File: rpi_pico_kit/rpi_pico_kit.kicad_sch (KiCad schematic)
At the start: 29 parts, among them J1 Barrel_Jack_Switch, J2 Conn_01x03_Male, Q1 BC807, Q2 BC807, SW1 SW_Push, U1 RPi Pico

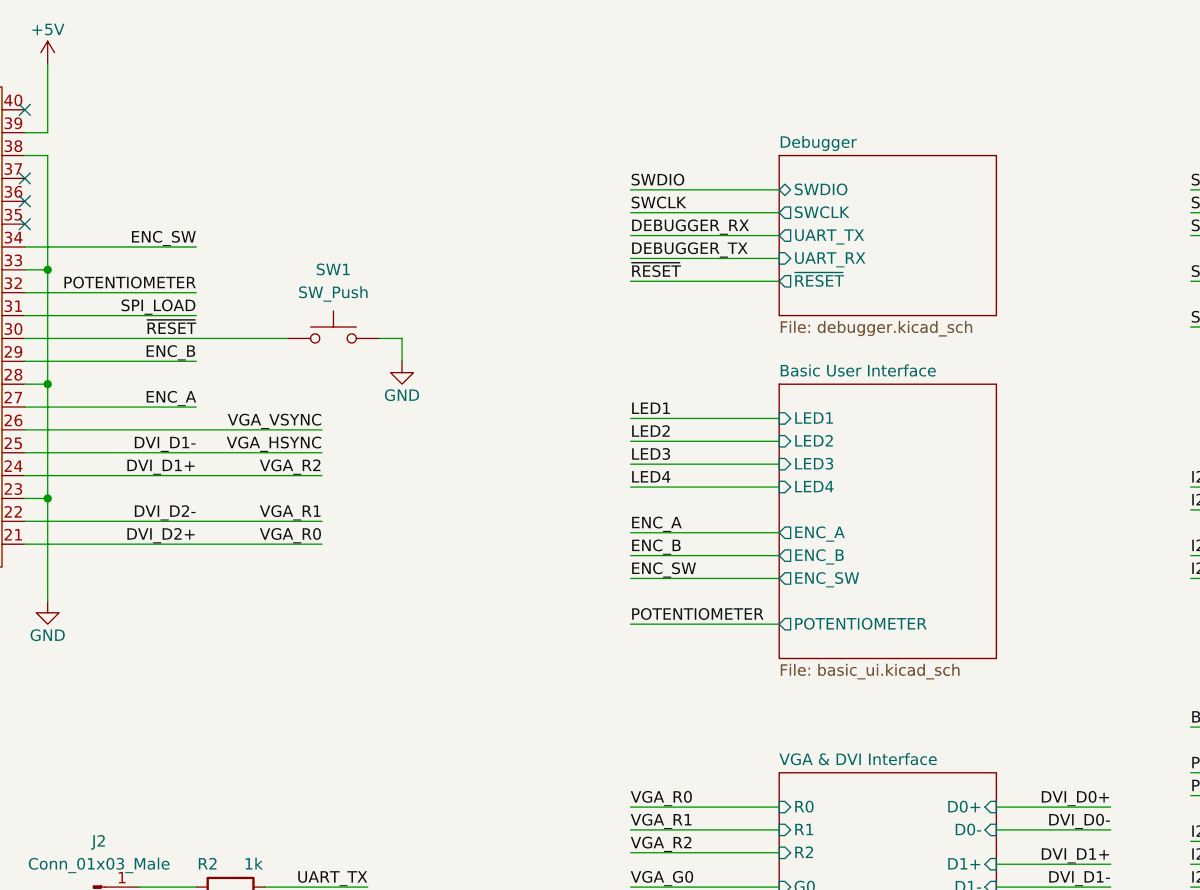
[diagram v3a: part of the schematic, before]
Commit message: added dac buttons
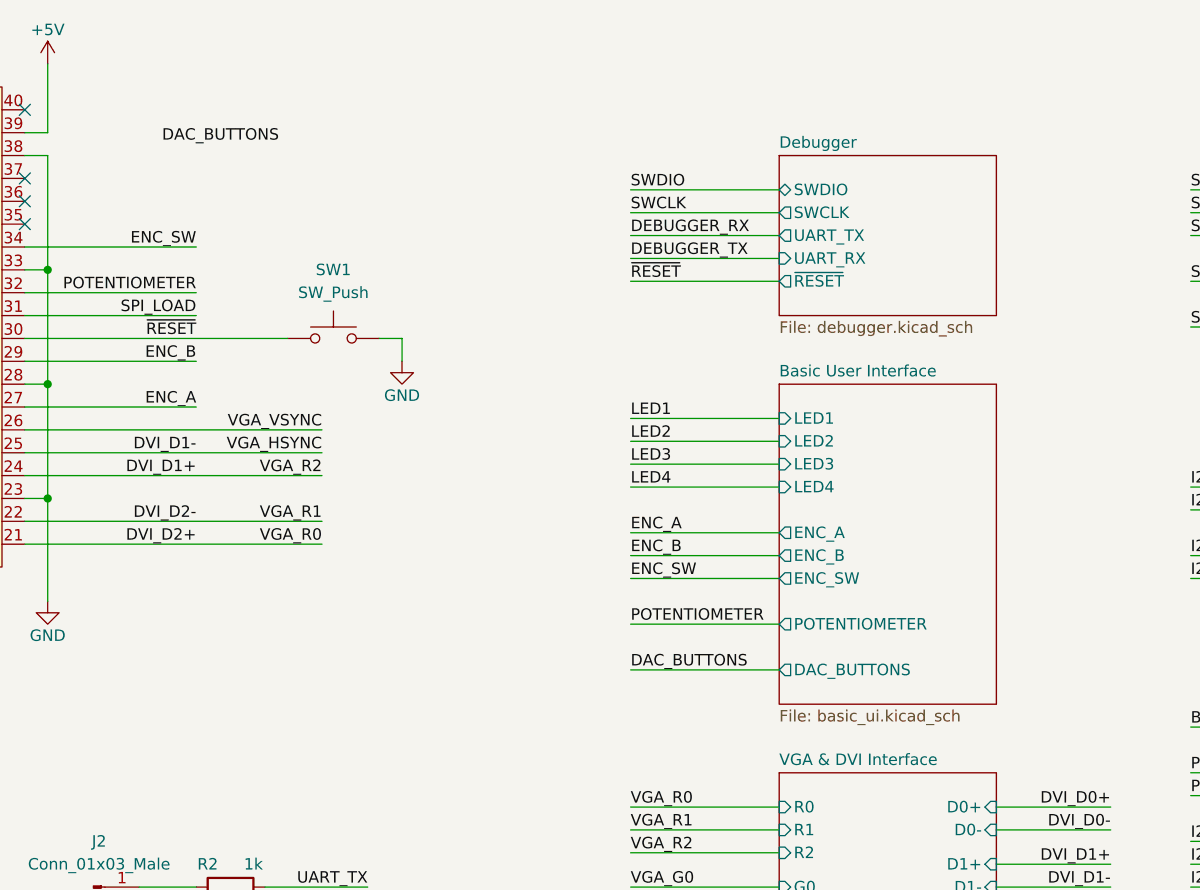
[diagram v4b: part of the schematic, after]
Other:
- sheet Basic User Interface ports: added DAC_BUTTONS; removed none
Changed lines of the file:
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@@
+    (stroke (width 0) (type default))
+  )
+  (wire (pts (xy 171.45 91.44) (xy 187.96 91.44))
     (stroke (width 0) (type default))
   )
@@
     (effects (font (size 1.27 1.27)) (justify left bottom))
   )
+  (label "DAC_BUTTONS" (at 171.45 91.44 0) (fields_autoplaced)
+    (effects (font (size 1.27 1.27)) (justify left bottom))
+  )
   (label "I2S_DIN" (at 53.34 62.23 0) (fields_autoplaced)
     (effects (font (size 1.27 1.27)) (justify left bottom))
   )
   (label "LED3" (at 27.94 54.61 0) (fields_autoplaced)
+    (effects (font (size 1.27 1.27)) (justify left bottom))
+  )
+  (label "DAC_BUTTONS" (at 119.38 33.02 0) (fields_autoplaced)
     (effects (font (size 1.27 1.27)) (justify left bottom))
   )
@@
     )
   )
-  (sheet (at 187.96 59.69) (size 24.13 30.48) (fields_autoplaced)
+  (sheet (at 187.96 59.69) (size 24.13 35.56) (fields_autoplaced)
     (stroke (width 0.1524) (type solid))
     (fill (color 0 0 0 0.0000))
@@
       (effects (font (size 1.27 1.27)) (justify left bottom))
     )
-    (property "Sheetfile" "basic_ui.kicad_sch" (id 1) (at 187.96 90.7546 0)
+    (property "Sheetfile" "basic_ui.kicad_sch" (id 1) (at 187.96 95.8346 0)
       (effects (font (size 1.27 1.27)) (justify left top))
     )
@@
     )
     (pin "LED4" input (at 187.96 71.12 180)
+      (effects (font (size 1.27 1.27)) (justify left))
+    )
+    (pin "DAC_BUTTONS" output (at 187.96 91.44 180)
       (effects (font (size 1.27 1.27)) (justify left))
     )
@@
       (reference "#PWR0147") (unit 1) (value "+5V") (footprint "")
     )
+    (path "/81612aa8-1e7d-439d-a45b-52594d29b291/1f6ded43-9f8d-4c63-8d4b-0b4527732d33"
+      (reference "#PWR?") (unit 1) (value "GND") (footprint "")
+    )
+    (path "/81612aa8-1e7d-439d-a45b-52594d29b291/4a31351e-1acf-47a2-a2c6-af92ae80f078"
+      (reference "#PWR?") (unit 1) (value "+3.3V") (footprint "")
+    )
+    (path "/81612aa8-1e7d-439d-a45b-52594d29b291/6f3c9916-5dd9-4b05-a345-f5527efc569b"
+      (reference "#PWR?") (unit 1) (value "+3.3V") (footprint "")
+    )
+    (path "/81612aa8-1e7d-439d-a45b-52594d29b291/89d0b3a4-37ce-4d00-9351-a681f8038582"
+      (reference "#PWR?") (unit 1) (value "GND") (footprint "")
+    )
+    (path "/81612aa8-1e7d-439d-a45b-52594d29b291/91069285-3fa6-4ca9-adec-5c5881e6c697"
+      (reference "#PWR?") (unit 1) (value "+3.3V") (footprint "")
+    )
+    (path "/81612aa8-1e7d-439d-a45b-52594d29b291/93d31bcb-10f6-4d54-bcae-9ef54872bd7b"
+      (reference "#PWR?") (unit 1) (value "+3.3V") (footprint "")
+    )
+    (path "/81612aa8-1e7d-439d-a45b-52594d29b291/ccea0e9a-8628-441a-ad2f-eb21f69a892a"
+      (reference "#PWR?") (unit 1) (value "+3.3V") (footprint "")
+    )
+    (path "/81612aa8-1e7d-439d-a45b-52594d29b291/f1a935b6-4bab-4abf-939e-7e028c183d62"
+      (reference "#PWR?") (unit 1) (value "GND") (footprint "")
+    )
     (path "/2bd19bd1-2975-4b91-a884-8b1113539e97/a927f1f4-98ba-40b8-bb8d-0eaab95070e5"
       (reference "BZ1") (unit 1) (value "Buzzer") (footprint "")
@@
       (reference "R89") (unit 1) (value "10k") (footprint "Resistor_SMD:R_0805_2012Metric_Pad1.20x1.40mm_HandSolder")
     )
+    (path "/81612aa8-1e7d-439d-a45b-52594d29b291/1ccb7d27-d1f4-4fcf-8a7f-33401111202f"
+      (reference "R?") (unit 1) (value "2k") (footprint "Resistor_SMD:R_0805_2012Metric_Pad1.20x1.40mm_HandSolder")
+    )
+    (path "/81612aa8-1e7d-439d-a45b-52594d29b291/39d89e3b-dd07-4df3-a868-bac27e6d5d7e"
+      (reference "R?") (unit 1) (value "1k") (footprint "Resistor_SMD:R_0805_2012Metric_Pad1.20x1.40mm_HandSolder")
+    )
+    (path "/81612aa8-1e7d-439d-a45b-52594d29b291/3c63107b-5d02-4b12-beac-ffe711ccd42d"
+      (reference "R?") (unit 1) (value "2k") (footprint "Resistor_SMD:R_0805_2012Metric_Pad1.20x1.40mm_HandSolder")
+    )
+    (path "/81612aa8-1e7d-439d-a45b-52594d29b291/42e543ad-9542-439b-9ff0-36e26f10ac03"
+      (reference "R?") (unit 1) (value "1k") (footprint "Resistor_SMD:R_0805_2012Metric_Pad1.20x1.40mm_HandSolder")
+    )
+    (path "/81612aa8-1e7d-439d-a45b-52594d29b291/4f8cb727-e4f9-46df-b234-ffef72cf20e7"
+      (reference "R?") (unit 1) (value "1k") (footprint "Resistor_SMD:R_0805_2012Metric_Pad1.20x1.40mm_HandSolder")
+    )
+    (path "/81612aa8-1e7d-439d-a45b-52594d29b291/5afb1b53-edfe-444c-9875-f83bd7c4a79d"
+      (reference "R?") (unit 1) (value "1k") (footprint "Resistor_SMD:R_0805_2012Metric_Pad1.20x1.40mm_HandSolder")
+    )
+    (path "/81612aa8-1e7d-439d-a45b-52594d29b291/6c7cd42a-7061-4c4b-9b98-0416e8fc4942"
+      (reference "R?") (unit 1) (value "2k") (footprint "Resistor_SMD:R_0805_2012Metric_Pad1.20x1.40mm_HandSolder")
+    )
+    (path "/81612aa8-1e7d-439d-a45b-52594d29b291/930f9912-8993-4e09-a189-56f2af054baf"
+      (reference "R?") (unit 1) (value "2k") (footprint "Resistor_SMD:R_0805_2012Metric_Pad1.20x1.40mm_HandSolder")
+    )
+    (path "/81612aa8-1e7d-439d-a45b-52594d29b291/c31321a7-a23c-41d8-914c-d144675613f4"
+      (reference "R?") (unit 1) (value "1k") (footprint "Resistor_SMD:R_0805_2012Metric_Pad1.20x1.40mm_HandSolder")
+    )
+    (path "/81612aa8-1e7d-439d-a45b-52594d29b291/cef2fd18-09ac-4f1b-8146-114e1991c8c7"
+      (reference "R?") (unit 1) (value "1k") (footprint "Resistor_SMD:R_0805_2012Metric_Pad1.20x1.40mm_HandSolder")
+    )
+    (path "/81612aa8-1e7d-439d-a45b-52594d29b291/e207b25f-a59c-43cc-b016-0dae5a5059ef"
+      (reference "R?") (unit 1) (value "2k") (footprint "Resistor_SMD:R_0805_2012Metric_Pad1.20x1.40mm_HandSolder")
+    )
+    (path "/81612aa8-1e7d-439d-a45b-52594d29b291/ef3534a4-6f90-4e7a-8bb9-e00ba3d1809e"
+      (reference "R?") (unit 1) (value "1k") (footprint "Resistor_SMD:R_0805_2012Metric_Pad1.20x1.40mm_HandSolder")
+    )
     (path "/81612aa8-1e7d-439d-a45b-52594d29b291/1911cdc8-cf7d-4aba-aec2-0c4898a95145"
       (reference "RV1") (unit 1) (value "10k") (footprint "Potentiometer_THT:Potentiometer_Alpha_RD901F-40-00D_Single_Vertical")
@@
       (reference "SW10") (unit 1) (value "SW") (footprint "")
     )
+    (path "/81612aa8-1e7d-439d-a45b-52594d29b291/1b2c612a-82c6-419c-a460-123d68d93bea"
+      (reference "SW?") (unit 1) (value "SW_Push_Dual") (footprint "")
+    )
+    (path "/81612aa8-1e7d-439d-a45b-52594d29b291/546fa5a6-58a0-41a6-8c07-4e51068d248d"
+      (reference "SW?") (unit 1) (value "SW_Push_Dual") (footprint "")
+    )
+    (path "/81612aa8-1e7d-439d-a45b-52594d29b291/b9b508d4-92cf-486d-9c6b-64ddc6ae2319"
+      (reference "SW?") (unit 1) (value "SW_Push_Dual") (footprint "")
+    )
+    (path "/81612aa8-1e7d-439d-a45b-52594d29b291/d433ac35-8aec-4df4-a695-67eb7fd1628e"
+      (reference "SW?") (unit 1) (value "SW_Push_Dual") (footprint "")
+    )
     (path "/8f624921-0bb1-4d0e-848b-7458a506535e"
       (reference "U1") (unit 1) (value "RPi Pico") (footprint "RPi_Pico:RPi_Pico_SMD_TH")
@@
       (reference "U10") (unit 1) (value "AT24CS32") (footprint "Package_SO:SOIC-8_3.9x4.9mm_P1.27mm")
     )
+    (path "/81612aa8-1e7d-439d-a45b-52594d29b291/e16cf771-c3fa-4172-bf01-32417bd59f0d"
+      (reference "U?") (unit 1) (value "74HC14") (footprint "")
+    )
+    (path "/81612aa8-1e7d-439d-a45b-52594d29b291/2270ceca-614b-44d8-b973-22cc22acb1a1"
+      (reference "U?") (unit 2) (value "74HC14") (footprint "")
+    )
+    (path "/81612aa8-1e7d-439d-a45b-52594d29b291/ce3284f3-a343-4acc-ac4c-24b15f7cfe2f"
+      (reference "U?") (unit 3) (value "74HC14") (footprint "")
+    )
+    (path "/81612aa8-1e7d-439d-a45b-52594d29b291/c7add3a9-d8c5-4a04-a5dc-a9dba744441f"
+      (reference "U?") (unit 4) (value "74HC14") (footprint "")
+    )
+    (path "/81612aa8-1e7d-439d-a45b-52594d29b291/c25647b1-45e8-4f2e-a8c5-1996e742f60f"
+      (reference "U?") (unit 5) (value "74HC14") (footprint "")
+    )
+    (path "/81612aa8-1e7d-439d-a45b-52594d29b291/edef7cb7-10cb-452e-b2c4-03db0c2096da"
+      (reference "U?") (unit 6) (value "74HC14") (footprint "")
+    )
+    (path "/81612aa8-1e7d-439d-a45b-52594d29b291/f55351c8-fcb1-4b7e-a6b3-0587524efc00"
+      (reference "U?") (unit 7) (value "74HC14") (footprint "")
+    )
     (path "/fe15dc26-52fc-427e-8179-2b8bb41b57bb/1c80ac80-63bf-4b8f-8b0a-dba59c0d317e"

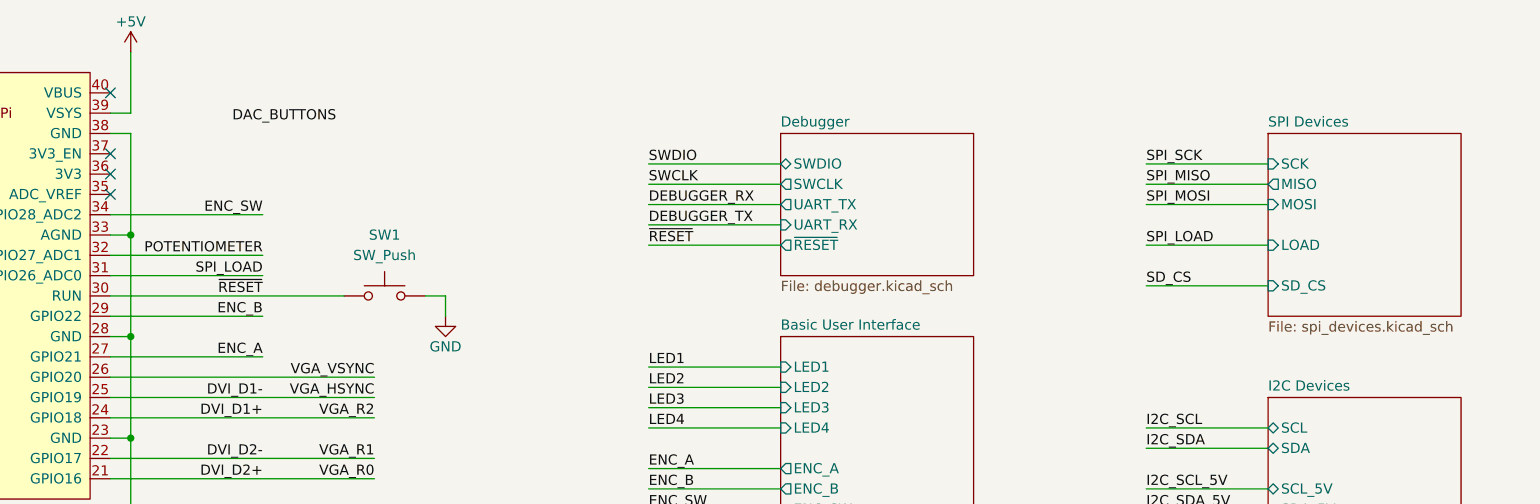
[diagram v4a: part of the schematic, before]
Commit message: replaced spi expander
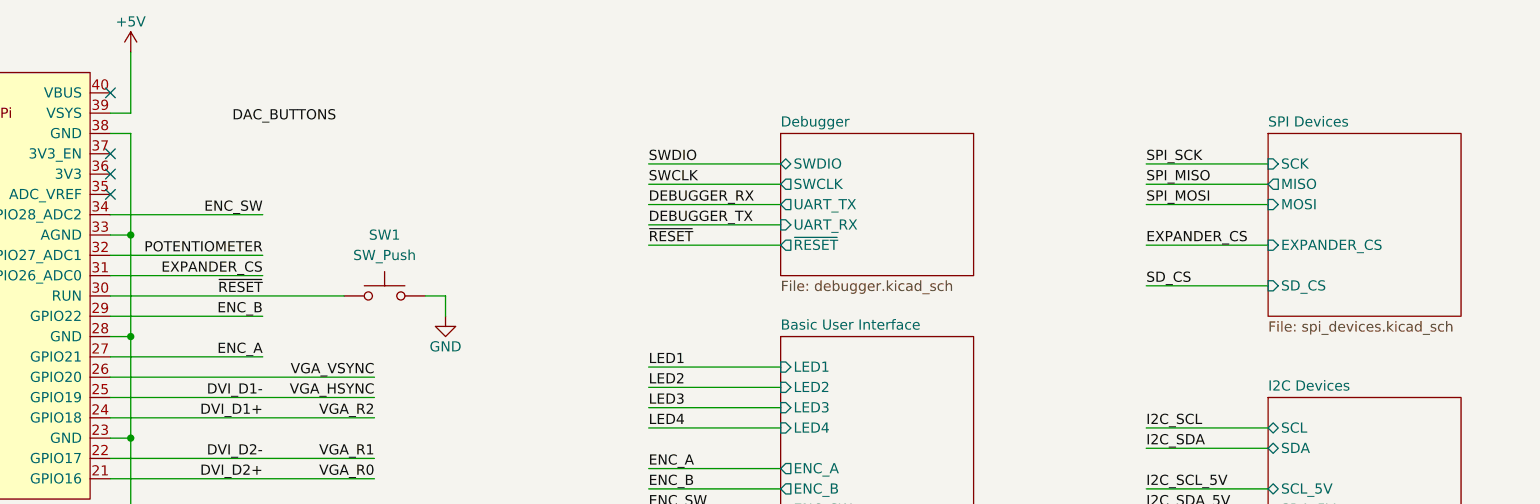
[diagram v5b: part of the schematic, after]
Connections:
- net SPI_LOAD renamed EXPANDER_CS
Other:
- sheet SPI Devices ports: added EXPANDER_CS; removed LOAD

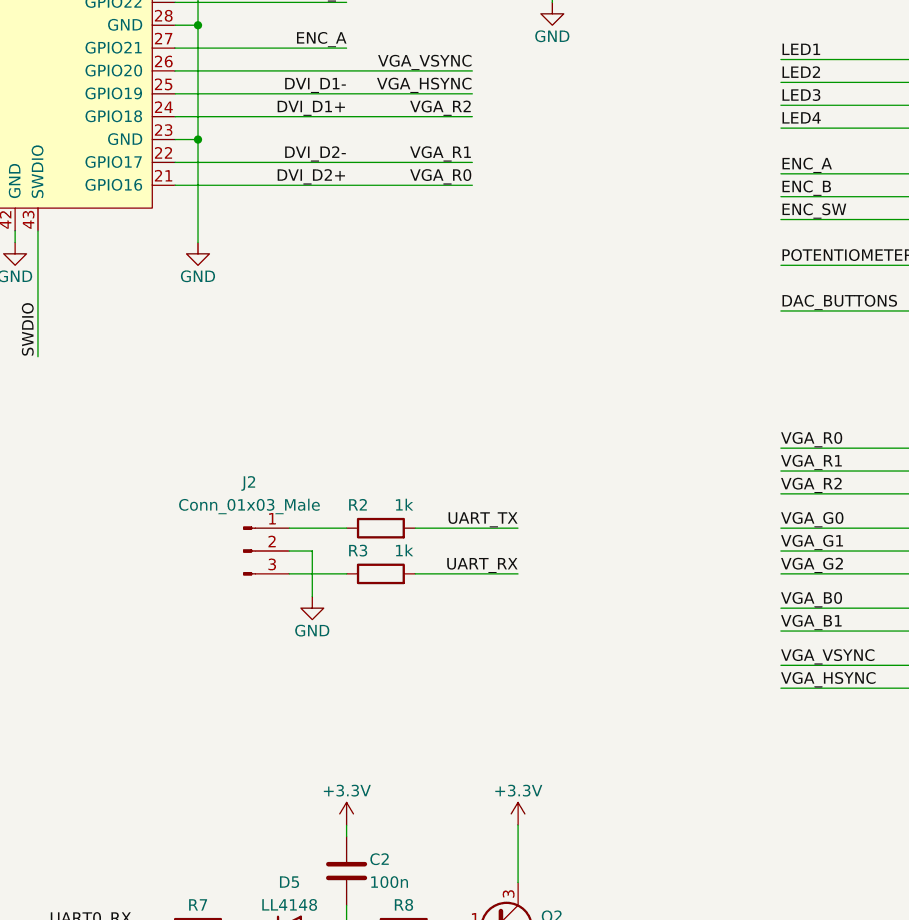
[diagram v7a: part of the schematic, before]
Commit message: added i2c level shifters
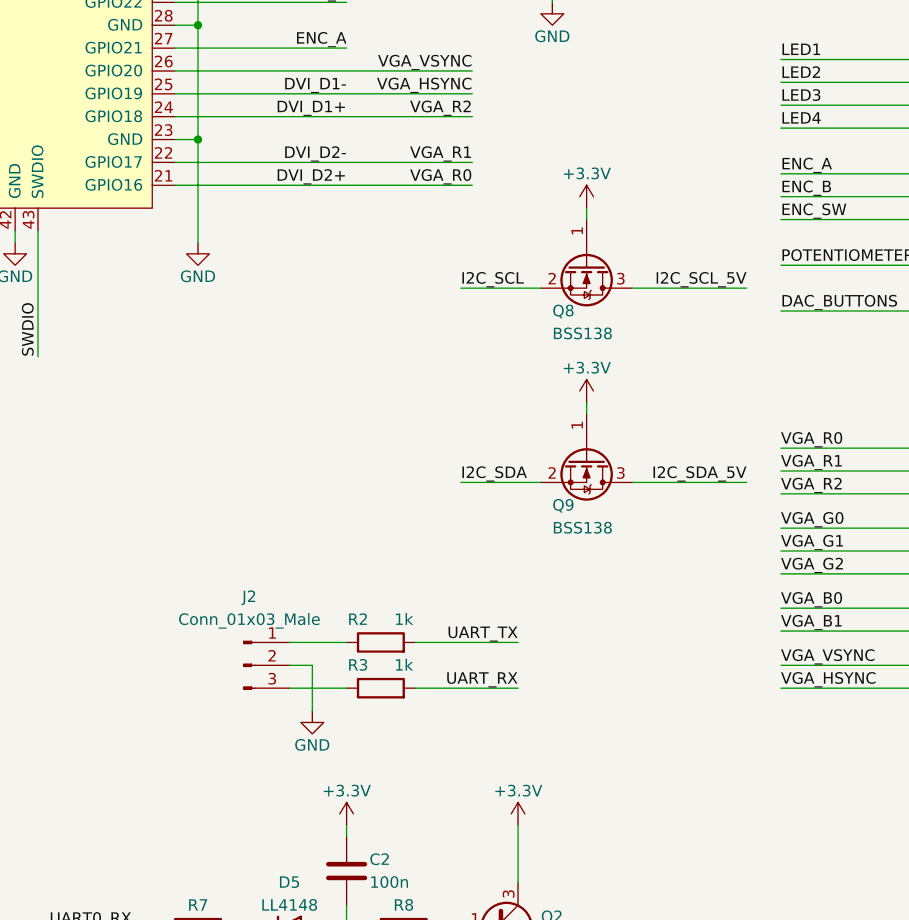
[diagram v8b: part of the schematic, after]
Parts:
- added Q8, Q9: BSS138, Package_TO_SOT_SMD:SOT-23, symbol Transistor_FET:BSS138
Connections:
- net +3V3: now also Q8.1 (G), Q9.1 (G)
- net I2C_SCL: now also Q8.2 (S)
- net I2C_SCL_5V: now also Q8.3 (D)
- net I2C_SDA: now also Q9.2 (S)
- net I2C_SDA_5V: now also Q9.3 (D)
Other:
- moved on the sheet: J2, R2, R3
